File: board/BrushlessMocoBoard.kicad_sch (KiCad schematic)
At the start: 0 parts

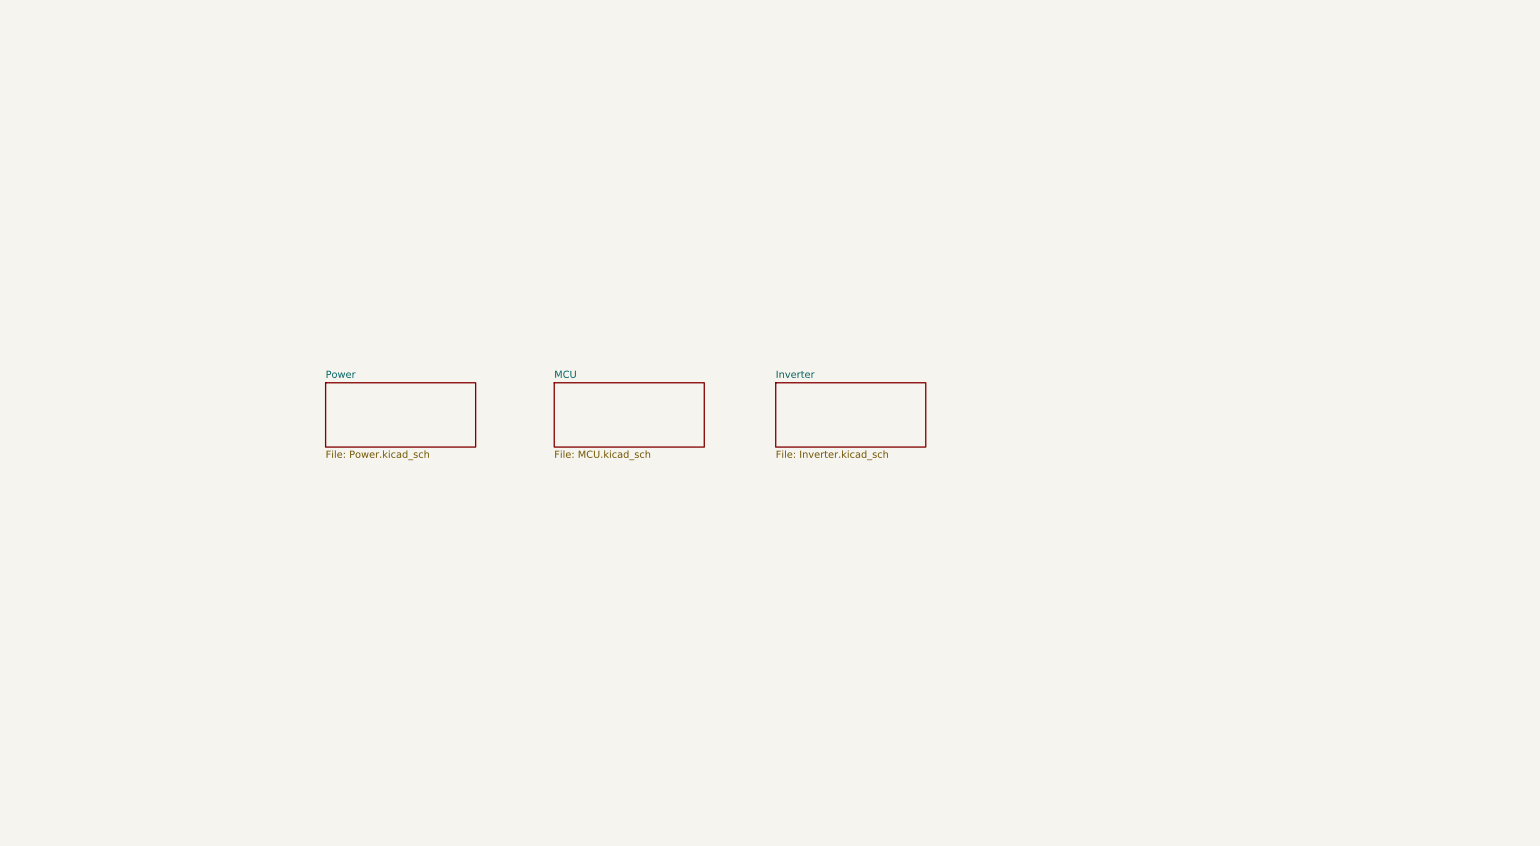
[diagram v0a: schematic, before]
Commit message: Began work on the schematic w/ CAN and buck application circuits.
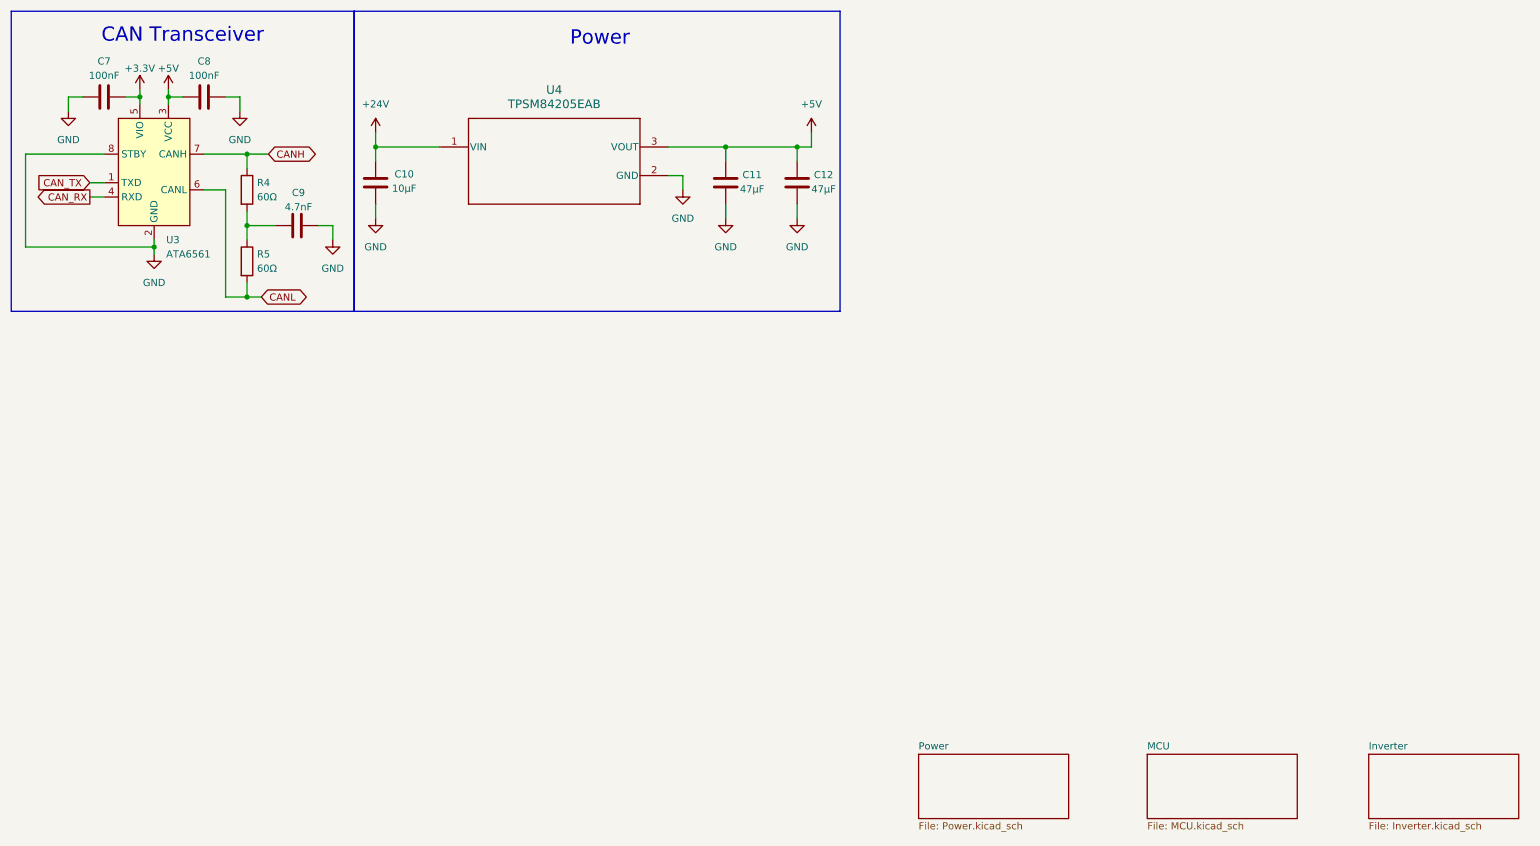
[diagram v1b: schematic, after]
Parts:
- added C10: 10μF, symbol Device:C
- added C11, C12: 47μF, symbol Device:C
- added C7, C8: 100nF, symbol Device:C
- added C9: 4.7nF, symbol Device:C
- added R4, R5: 60Ω, symbol Device:R
- added U3: ATA6561, Package_SO:SOIC-8_3.9x4.9mm_P1.27mm, symbol MRDT_Devices:ATA6561
- added U4: TPSM84205EAB, EAB0003A, symbol TPSM84205:TPSM84205EAB
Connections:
- new net: C9.1, R4.2, R5.1
- new net +24V: C10.1, U4.1 (VIN)
- new net +3.3V: C7.2, U3.5 (VIO)
- new net +5V: C11.1, C12.1, C8.1, U3.3 (VCC), U4.3 (VOUT)
- new net CANH: R4.1, U3.7 (CANH)
- new net CANL: R5.2, U3.6 (CANL)
- new net CAN_RX: U3.4 (RXD)
- new net CAN_TX: U3.1 (TXD)
- new net GND: C10.2, C11.2, C12.2, C7.1, C8.2, C9.2, U3.2 (GND), U3.8 (STBY), U4.2 (GND)
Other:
- note added: "CAN Transceiver"
- note added: "Power"

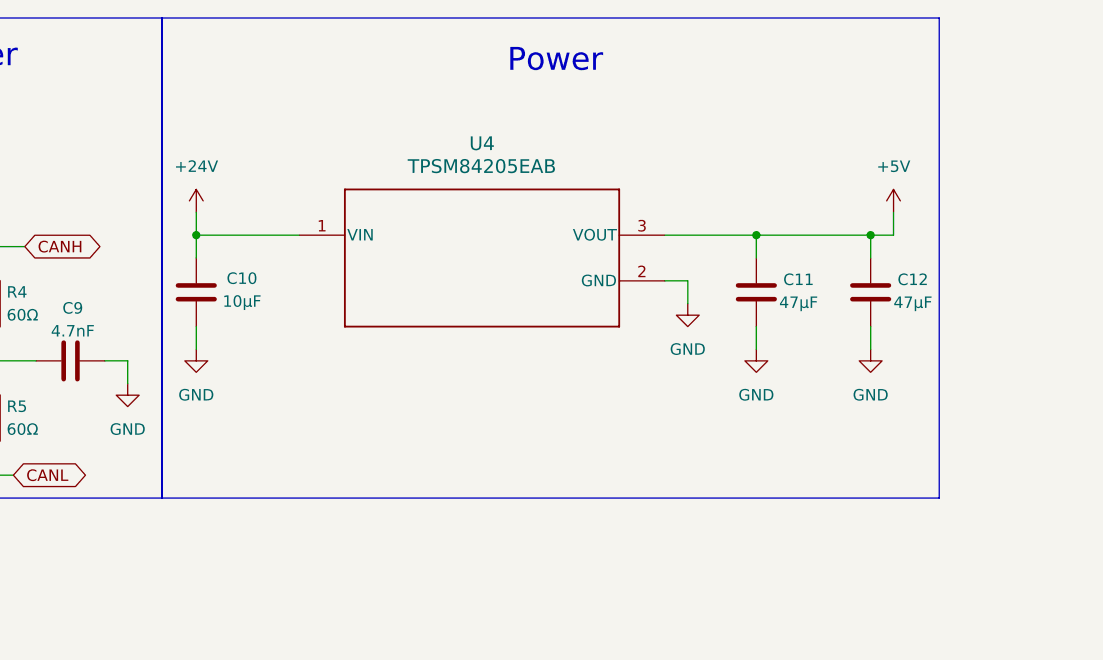
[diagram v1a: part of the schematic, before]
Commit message: Swapped buck to OKI
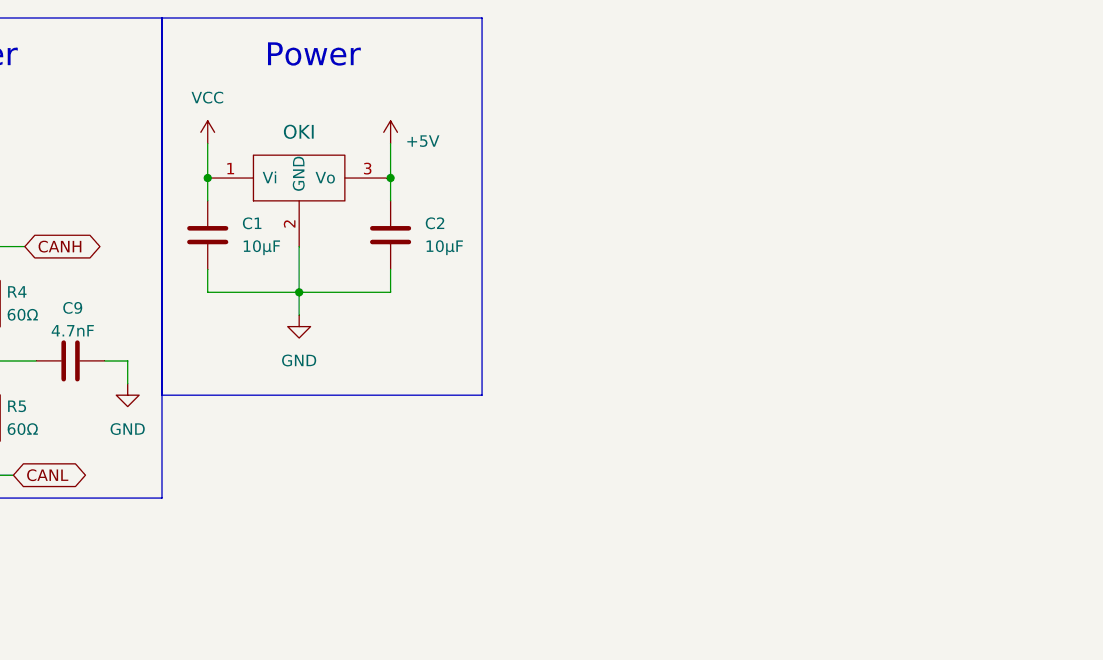
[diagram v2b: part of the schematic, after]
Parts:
- removed C10: 10μF, symbol Device:C
- removed C11, C12: 47μF, symbol Device:C
- removed U4: TPSM84205EAB, EAB0003A, symbol TPSM84205:TPSM84205EAB
- added C1: 10µF, Capacitor_SMD:C_1206_3216Metric_Pad1.33x1.80mm_HandSolder, symbol Device:C
- added C2: 10µF, Capacitor_SMD:C_0603_1608Metric_Pad1.08x0.95mm_HandSolder, symbol Device:C
- added U1: OKI, MRDT_Devices:OKI_Horizontal, symbol MRDT_Devices:OKI
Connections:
- net +5V: now also C2.1, U1.3 (Vo)
- net GND: now also C1.2, C2.2, U1.2 (GND)
- new net VCC: C1.1, U1.1 (Vi)

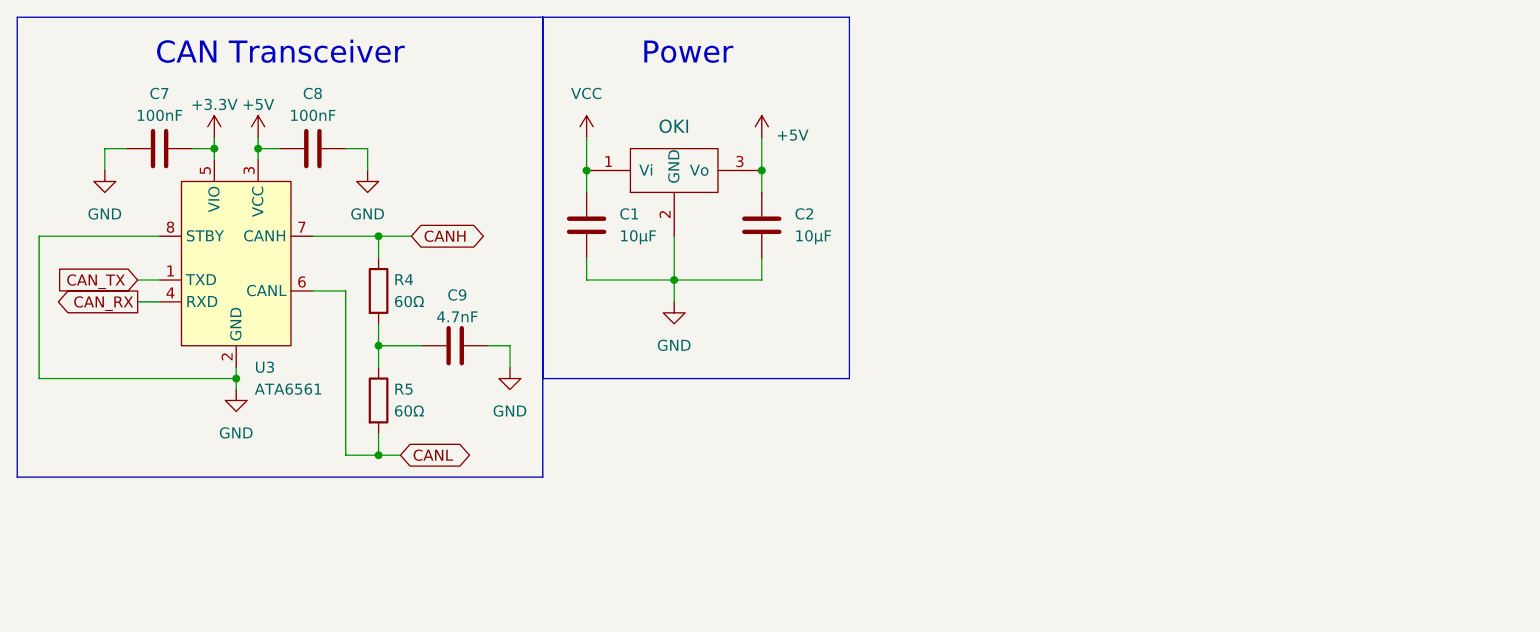
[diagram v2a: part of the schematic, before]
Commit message: Added MCU and initial half bridge circuits from application circuit.
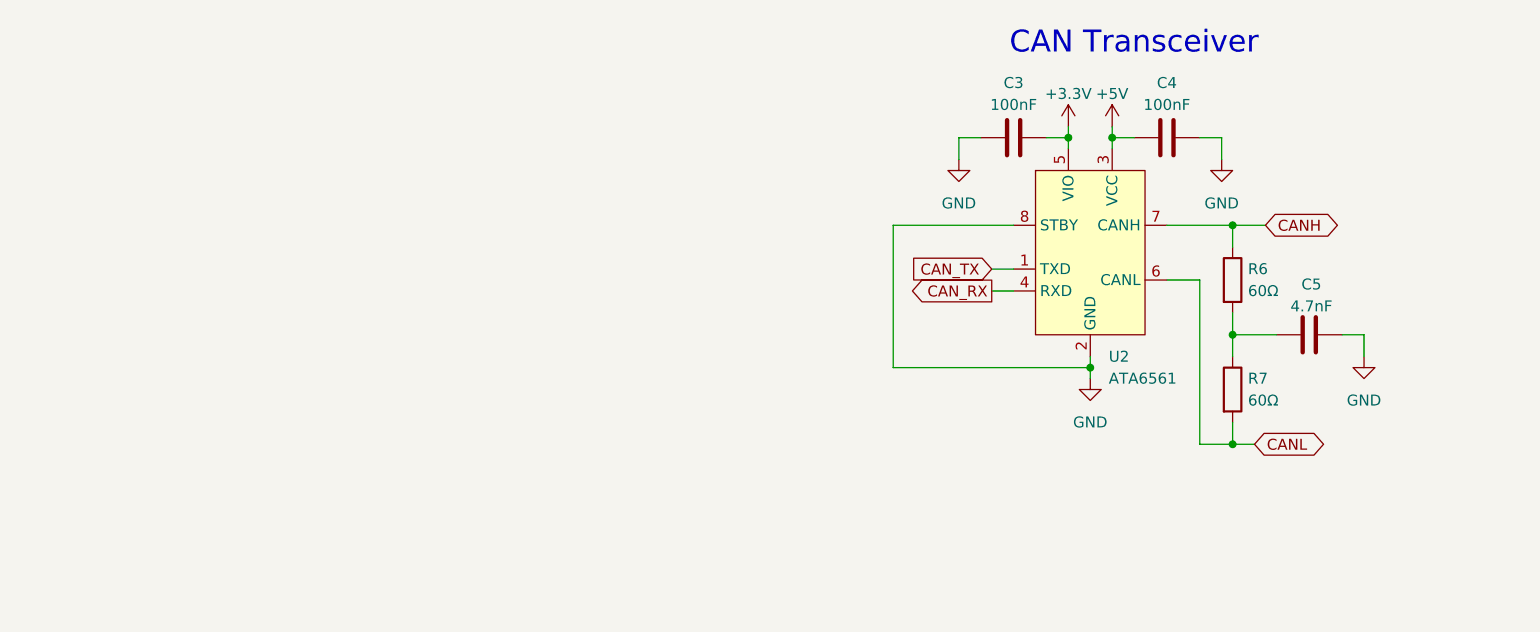
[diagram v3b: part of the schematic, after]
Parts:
- removed C1: 10µF, Capacitor_SMD:C_1206_3216Metric_Pad1.33x1.80mm_HandSolder, symbol Device:C
- removed C2: 10µF, Capacitor_SMD:C_0603_1608Metric_Pad1.08x0.95mm_HandSolder, symbol Device:C
- removed C7, C8: 100nF, symbol Device:C
- removed C9: 4.7nF, symbol Device:C
- removed R4, R5: 60Ω, symbol Device:R
- removed U1: OKI, MRDT_Devices:OKI_Horizontal, symbol MRDT_Devices:OKI
- removed U3: ATA6561, Package_SO:SOIC-8_3.9x4.9mm_P1.27mm, symbol MRDT_Devices:ATA6561
- added C3, C4: 100nF, symbol Device:C
- added C5: 4.7nF, symbol Device:C
- added R6, R7: 60Ω, symbol Device:R
- added U2: ATA6561, Package_SO:SOIC-8_3.9x4.9mm_P1.27mm, symbol MRDT_Devices:ATA6561
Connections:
- net +3.3V: now also C3.2, U2.5 (VIO)
- net +5V: now also C4.1, U2.3 (VCC)
- net CANH: now also R6.1, U2.7 (CANH)
- net CANL: now also R7.2, U2.6 (CANL)
- net CAN_RX: now also U2.4 (RXD)
- net CAN_TX: now also U2.1 (TXD)
- net GND: now also C3.1, C4.2, C5.2, U2.2 (GND), U2.8 (STBY)
- new net: C5.1, R6.2, R7.1
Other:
- note removed: "Power"

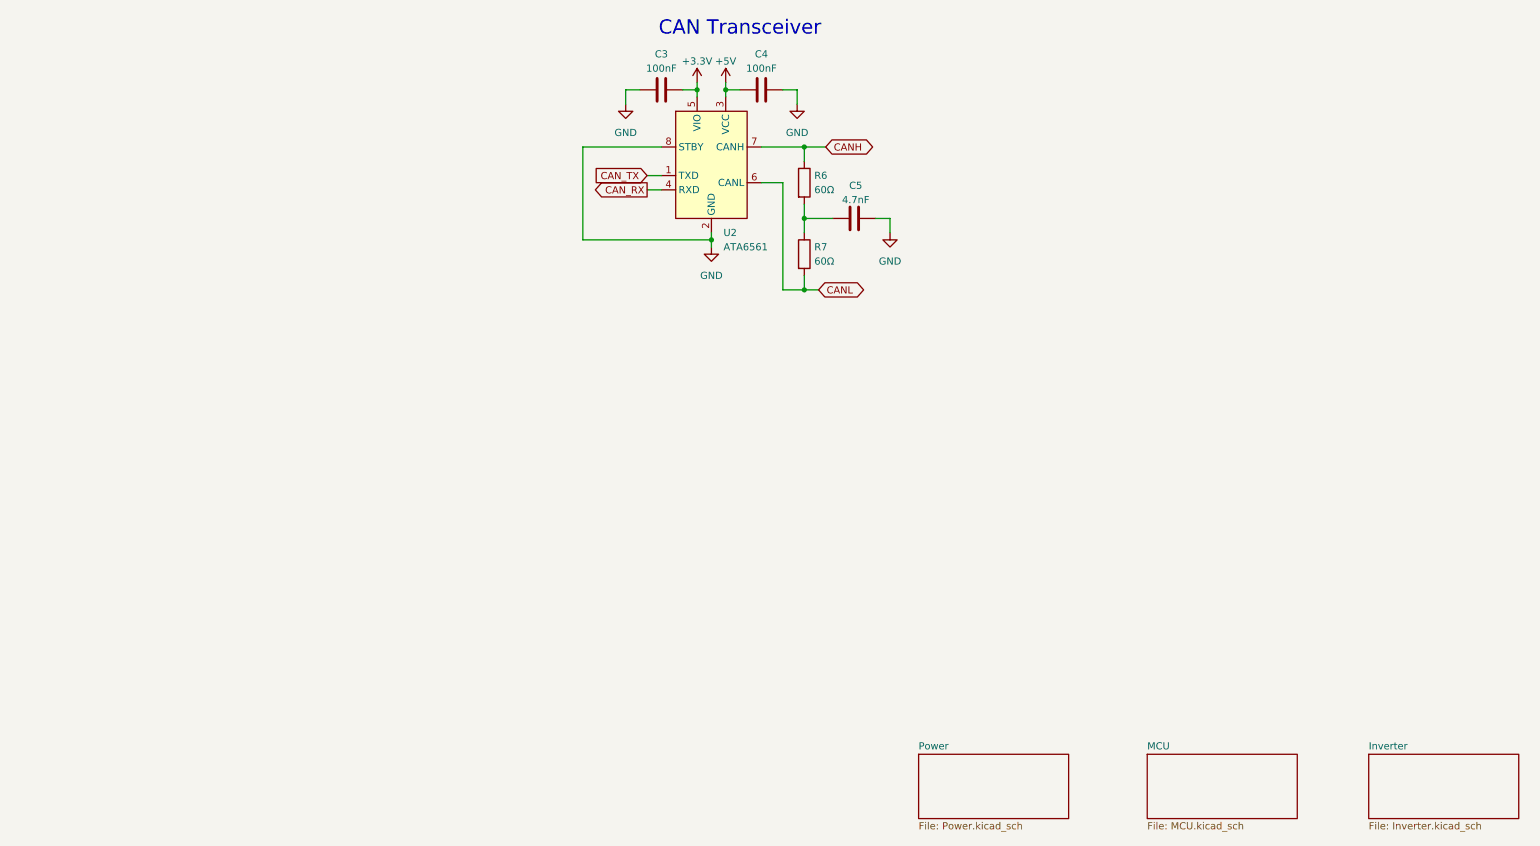
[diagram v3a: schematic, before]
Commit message: Completed basic application circuit from MCU datasheet and adjusted Hierarchical Paths.
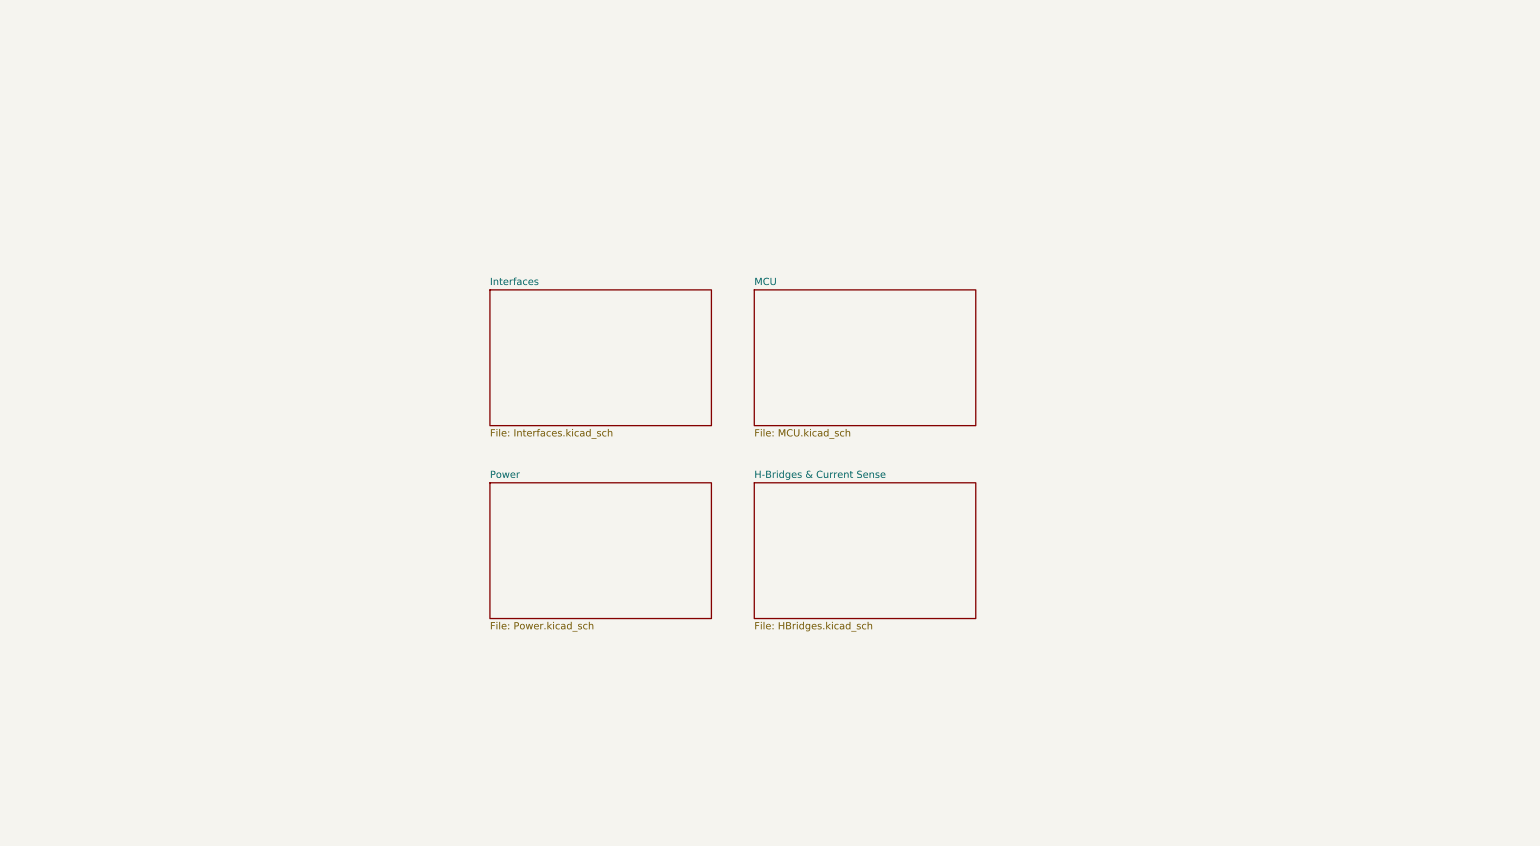
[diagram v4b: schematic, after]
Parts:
- removed C3, C4: 100nF, symbol Device:C
- removed C5: 4.7nF, symbol Device:C
- removed R6, R7: 60Ω, symbol Device:R
- removed U2: ATA6561, Package_SO:SOIC-8_3.9x4.9mm_P1.27mm, symbol MRDT_Devices:ATA6561
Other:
- sheet Inverter renamed H-Bridges & Current Sense
- added sheet Interfaces (Interfaces.kicad_sch)
- sheet H-Bridges & Current Sense: file Inverter.kicad_sch -> HBridges.kicad_sch
- note removed: "CAN Transceiver"

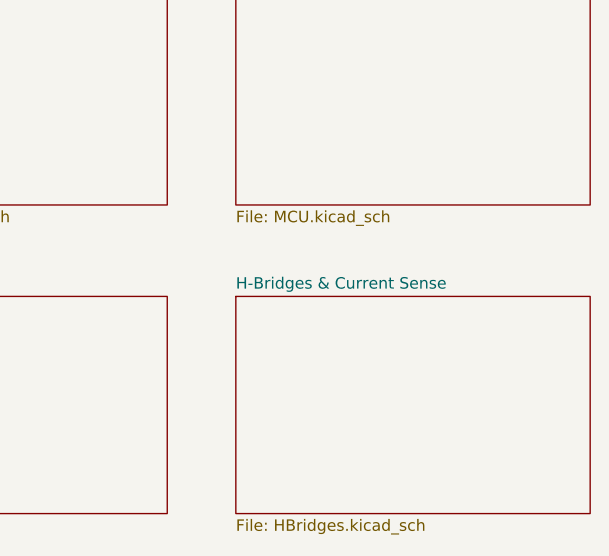
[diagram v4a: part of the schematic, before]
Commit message: Finished adding component values to circuits, except for 4 filtering capacitors
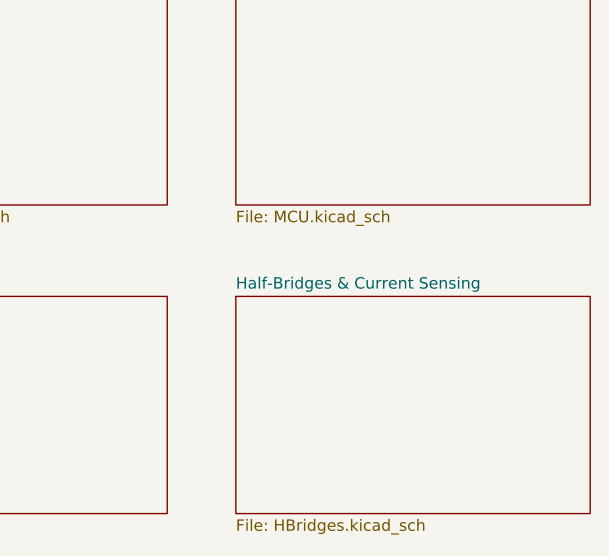
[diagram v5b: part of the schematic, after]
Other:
- sheet H-Bridges & Current Sense renamed Half-Bridges & Current Sensing
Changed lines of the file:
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@@
 			(color 0 0 0 0.0000)
 		)
-		(property "Sheetname" "H-Bridges & Current Sense"
+		(property "Sheetname" "Half-Bridges & Current Sensing"
 			(at 144.78 95.8084 0)
 			(effects
